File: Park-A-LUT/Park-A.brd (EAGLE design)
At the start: 45.1 x 30.5 mm, 38 parts, among them Q1 16MHz, T1 BC848SMD, T2 IRLML5203, T3 BC848SMD, T4 IRLML5203, U1 PIC18F25K80, U2 78M05, U3 TJA1055T

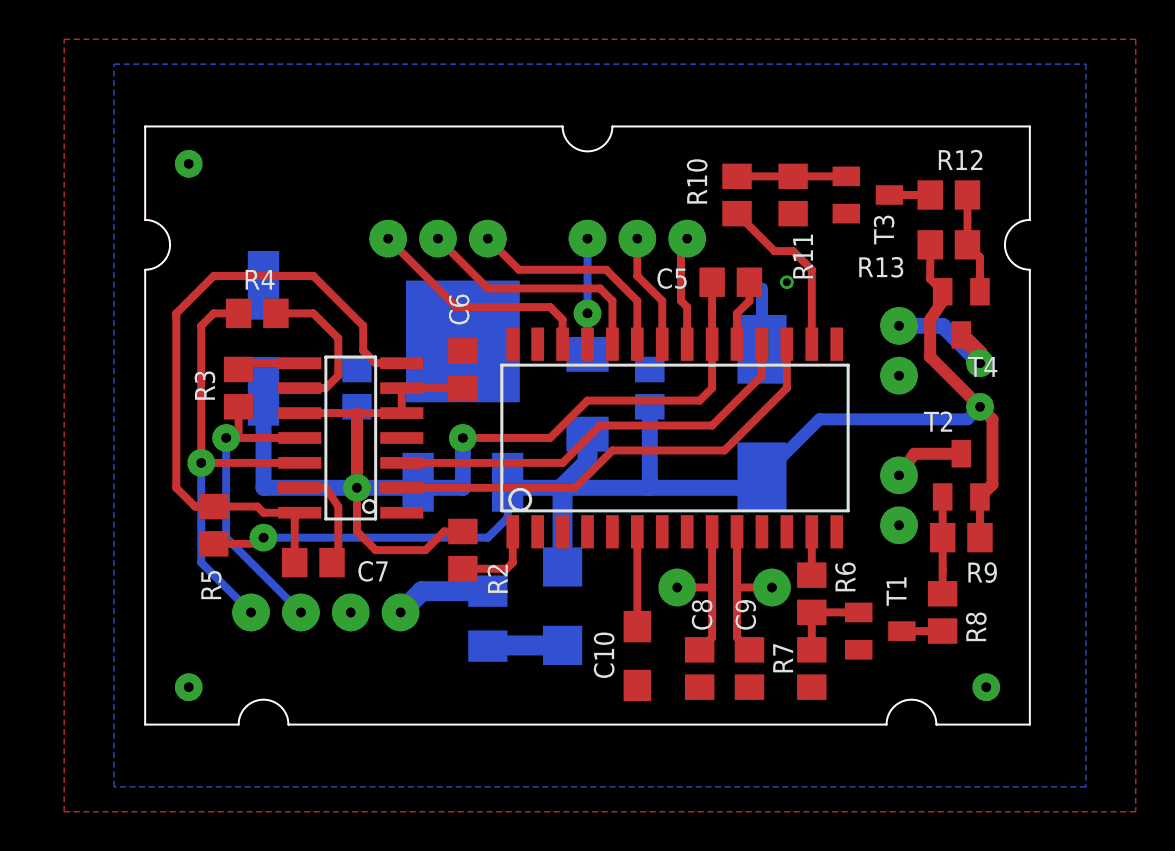
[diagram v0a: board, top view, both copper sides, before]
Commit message: Add ICSP
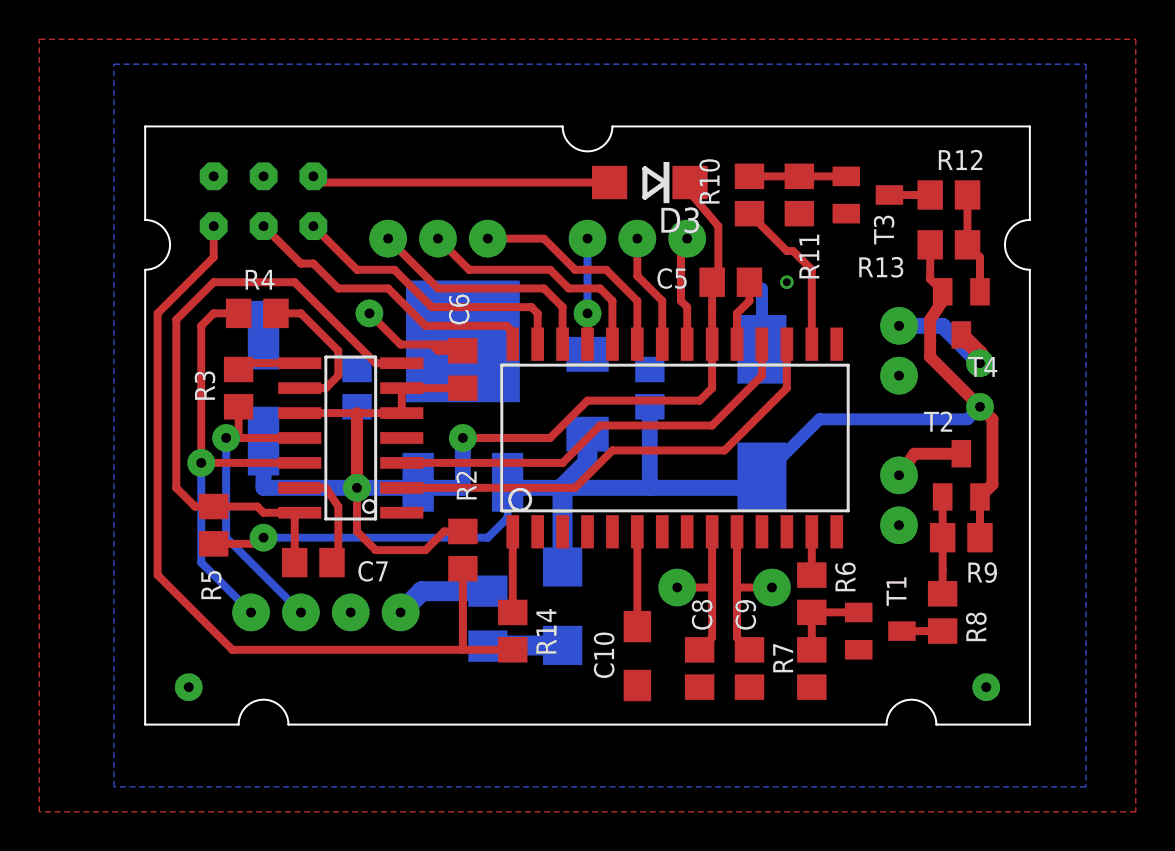
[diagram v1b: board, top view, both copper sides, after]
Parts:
- added D3: SS16, Park-A:DO214AC
- added JP1: (no value), Park-A:2X03
- added R14: 470, rcl:R0805
- moved C4 2.54 mm to (27.9, 57.1)
- moved R10 0.63 mm to (52.7, 67.0)
- moved R11 0.32 mm to (55.2, 67.0)
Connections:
- new net N$19: JP1.5, R14.1, R2.2
- new net N$20: D3.A, JP1.2
- net +5V: now also D3.C
- net GND: now also JP1.6
- net N$4: now also R14.2; no longer R2.2
- net PGC: now also JP1.1
- net PGD: now also JP1.3
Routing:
- net N$19: track 0.00 -> 42.8 mm
- net PGD: track 0.00 -> 15.6 mm
- net N$20: track 0.00 -> 15.2 mm
- net PGC: track 0.00 -> 14.8 mm
- net GND: track 12.2 -> 19.6 mm
- net +5V: track 62.9 -> 66.4 mm
- net N$6: track 33.2 -> 32.0 mm
- net N$16: track 5.57 -> 4.93 mm
- net N$15: track 8.79 -> 8.15 mm

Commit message: Small fixes
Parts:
- removed JP1: (no value), Park-A:2X03
- added C11: 0.1uF, rcl:C0805
- added ICSP: (no value), Park-A:2X03
- moved R14 0.71 mm to (41.3, 45.1), turned to 270 degrees
- moved R2 0.45 mm to (38.4, 49.2)
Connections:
- removed net N$19: JP1.5, R14.1, R2.2
- new net MCLR: ICSP.5, R14.2, U1.1
- net GND: now also C11.2, ICSP.6; no longer JP1.6
- net N$20: now also ICSP.2; no longer JP1.2
- net N$4: now also C11.1, R14.1, R2.2; no longer R14.2, U1.1
- net PGC: now also ICSP.1; no longer JP1.1
- net PGD: now also ICSP.3; no longer JP1.3
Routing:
- net MCLR: track 0.00 -> 51.8 mm
- net N$19: track 42.8 -> 0.00 mm
- net N$4: track 4.11 -> 5.09 mm
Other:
- outline, holes or cut-outs redrawn
- board text added: "TX RX RES"

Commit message: Small Fixes
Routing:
- net GND: track 19.6 -> 27.3 mm
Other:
- board text added: "+5"
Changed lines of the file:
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@@
 <layer number="46" name="Milling" color="3" fill="1" visible="no" active="yes"/>
 <layer number="47" name="Measures" color="7" fill="1" visible="no" active="yes"/>
-<layer number="48" name="Document" color="7" fill="1" visible="yes" active="yes"/>
+<layer number="48" name="Document" color="7" fill="1" visible="no" active="yes"/>
 <layer number="49" name="Reference" color="7" fill="1" visible="no" active="yes"/>
 <layer number="50" name="dxf" color="7" fill="1" visible="no" active="no"/>
@@
 <wire x1="30.7975" y1="63.1825" x2="23.495" y2="63.1825" width="0.4064" layer="42"/>
 <wire x1="23.495" y1="63.1825" x2="23.495" y2="63.8175" width="0.4064" layer="42"/>
+<text x="32.7025" y="67.6275" size="0.6096" layer="16" font="vector" rot="MR0">+5</text>
 </plain>
 <attributes>
@@
 <via x="64.77" y="41.91" extent="1-16" drill="0.5" diameter="1.4224"/>
 <wire x1="53.34" y1="59.13" x2="53.34" y2="62.23" width="0.6096" layer="16"/>
-<via x="54.61" y="62.5475" extent="1-16" drill="0.4"/>
+<via x="54.2925" y="62.5475" extent="1-16" drill="0.4" diameter="1.6764"/>
 <wire x1="38.1" y1="59.0525" x2="38.1" y2="59.055" width="0.4064" layer="1"/>
 <wire x1="36.51" y1="59.3725" x2="36.8275" y2="59.055" width="0.4064" layer="1"/>
@@
 <wire x1="34.925" y1="59.3725" x2="33.3375" y2="60.96" width="0.4064" layer="1"/>
 <contactref element="C11" pad="2"/>
+<wire x1="52.705" y1="62.5475" x2="53.0225" y2="62.5475" width="0.4064" layer="1"/>
+<wire x1="53.34" y1="62.5475" x2="53.6575" y2="62.5475" width="0.4064" layer="1"/>
+<wire x1="53.975" y1="62.5475" x2="54.2925" y2="62.5475" width="0.4064" layer="1"/>
+<wire x1="54.2925" y1="62.5475" x2="54.2925" y2="61.595" width="0.4064" layer="1"/>
+<wire x1="54.2925" y1="61.595" x2="53.975" y2="61.595" width="0.4064" layer="1"/>
+<wire x1="53.975" y1="61.595" x2="53.6575" y2="61.595" width="0.4064" layer="1"/>
+<wire x1="53.34" y1="61.595" x2="53.0225" y2="61.595" width="0.4064" layer="1"/>
+<wire x1="53.0225" y1="61.595" x2="53.0225" y2="62.5475" width="0.4064" layer="1"/>
+<wire x1="53.0225" y1="62.5475" x2="53.34" y2="62.5475" width="0.4064" layer="1"/>
+<wire x1="53.34" y1="62.5475" x2="53.34" y2="61.595" width="0.4064" layer="1"/>
+<wire x1="53.34" y1="61.595" x2="53.6575" y2="61.595" width="0.4064" layer="1"/>
+<wire x1="53.6575" y1="61.595" x2="53.6575" y2="62.5475" width="0.4064" layer="1"/>
+<wire x1="53.6575" y1="62.5475" x2="53.975" y2="62.5475" width="0.4064" layer="1"/>
+<wire x1="53.975" y1="62.5475" x2="53.975" y2="61.595" width="0.4064" layer="1"/>
 </signal>
 <signal name="+5V">
